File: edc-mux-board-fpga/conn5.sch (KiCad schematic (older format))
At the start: 24 parts, among them U19 MAX4910, U20 TLV320AIC3206, U21 P82B96

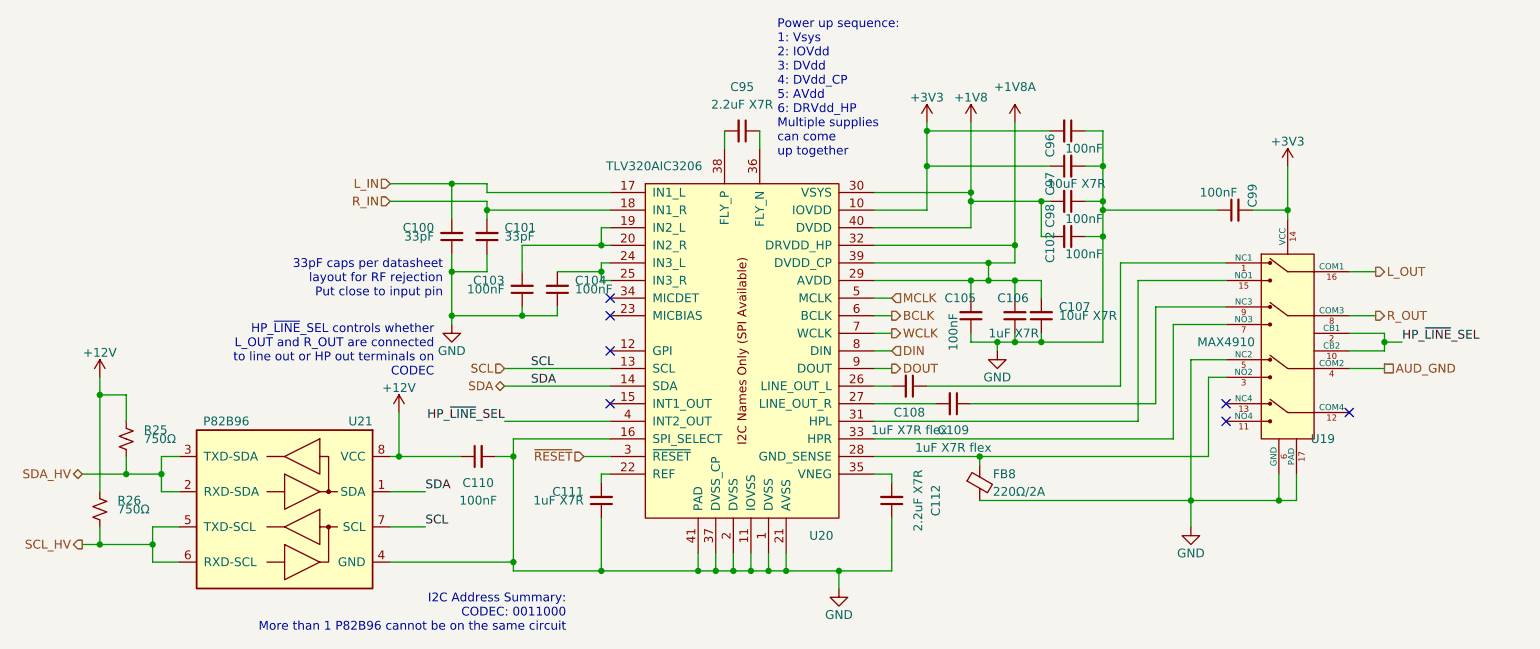
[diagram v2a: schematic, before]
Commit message: re-annotating after adding power ICs and decoupling capacitors.
Also verified most footprints, and updated schematic field data.
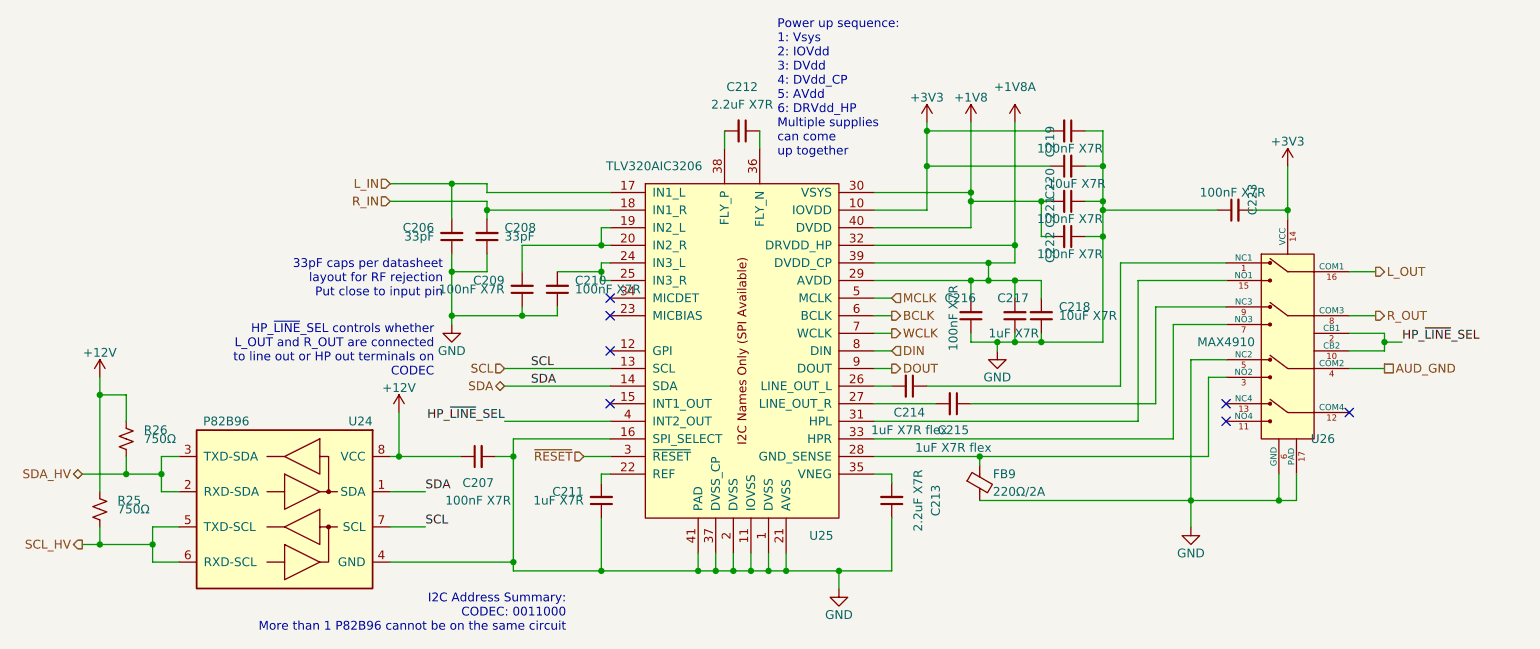
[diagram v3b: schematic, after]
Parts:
- C207: renamed from C110; value 100nF -> 100nF X7R
- C209: renamed from C103; value 100nF -> 100nF X7R
- C210: renamed from C104; value 100nF -> 100nF X7R
- C216: renamed from C105; value 100nF -> 100nF X7R
- C219: renamed from C96; value 100nF -> 100nF X7R
- C221: renamed from C98; value 100nF -> 100nF X7R
- C222: renamed from C102; value 100nF -> 100nF X7R
- C223: renamed from C99; value 100nF -> 100nF X7R
- R25: renamed from R26; Package ID (none) -> 0402in/1005mm
- R26: renamed from R25; Package ID (none) -> 0402in/1005mm
- renumbered C100 to C206, C101 to C208, C111 to C211, C95 to C212, C112 to C213, C108 to C214, C109 to C215, C106 to C217, C107 to C218, C97 to C220, FB8 to FB9, U21 to U24, U20 to U25, U19 to U26

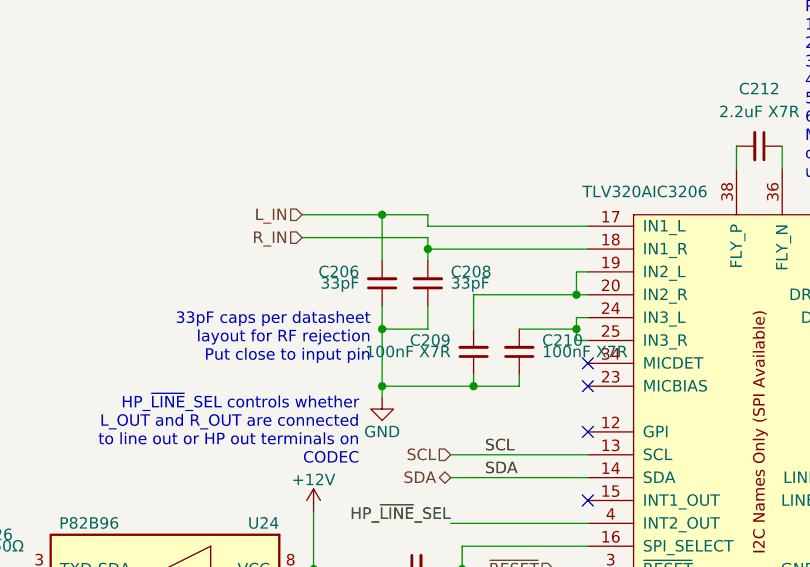
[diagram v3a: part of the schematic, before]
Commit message: Reannotating and adding more fields to components
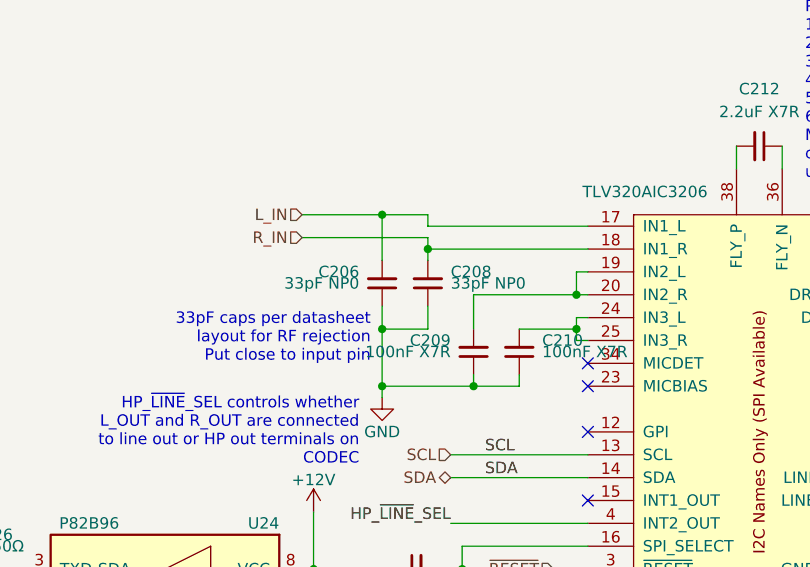
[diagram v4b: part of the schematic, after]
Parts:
- C206, C208: value 33pF -> 33pF NP0; footprint Capacitor_SMD:C_0603_1608Metric -> Capacitor_SMD:C_0402_1005Metric; Characteristics (none) -> CAP CER 33PF 25V NP0 0402; Description (none) -> MLCC Capacitor; Manufacturer (none) -> AVX; Manufacturers Part Number (none) -> 04023A330FAT2A; Package ID 0603in/1608mm -> 0402in/1005mm
- C207, C209, C210, C216, C219, C221, C222, C223: Characteristics (none) -> CAP CER 0.1UF 25V X7R 0603; Description (none) -> MLCC Capacitor; Manufacturer (none) -> Kemet; Manufacturers Part Number (none) -> C0603C104J3RACAUTO
- C211, C217: Characteristics (none) -> CAP CER 1UF 25V X7R 0603; Description (none) -> MLCC Capacitor
- C212, C213: footprint Capacitor_SMD:C_0603_1608Metric -> Capacitor_SMD:C_0805_2012Metric; Characteristics (none) -> CAP CER 2.2UF 25V X7R 0805; Description (none) -> MLCC Capacitor; Manufacturer (none) -> TDK; Manufacturers Part Number (none) -> CGA4J3X7R1E225K125AB; Package ID 0603in/1608mm -> 0805in/2012mm
- C214, C215: Characteristics (none) -> CAP CER 0805 1UF 25V X7R 5%; Description (none) -> MLCC Capacitor; Manufacturers Part Number C0805X105J3RACAUTO -> C0805X105J3RECAUTO
- C218, C220: Characteristics (none) -> CAP CER 10UF 25V X7R 1206; Description (none) -> MLCC Capacitor
- FB9: footprint Resistor_SMD:R_0603_1608Metric -> Inductor_SMD:L_0603_1608Metric; Description (none) -> Ferrite Bead
- R25, R26: Description (none) -> Resistor
- U24: Description (none) -> I2C Buffer / Voltage Translator; Manufacturer (none) -> Texas Instruments; Manufacturers Part Number (none) -> P82B96; Package ID (none) -> TSSOP8
- U25: Description (none) -> I2S Audio Codec; Manufacturer (none) -> Texas Instruments; Package ID (none) -> UQFN40
- U26: Description (none) -> Clickless Audio Switch; Manufacturer (none) -> Maxim Integrated; Package ID (none) -> TQFN16

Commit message: Fixed resistor footprint
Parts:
- R25, R26: footprint Resistor_SMD:R_0603_1608Metric -> Resistor_SMD:R_0402_1005Metric
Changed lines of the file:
@@
 F 0 "R26" H 1800 3950 50  0000 L CNN
 F 1 "750Ω" H 1800 3900 50  0000 L CNN
-F 2 "Resistor_SMD:R_0603_1608Metric" H 1700 3900 50  0001 C CNN
+F 2 "Resistor_SMD:R_0402_1005Metric" H 1700 3900 50  0001 C CNN
 F 3 "~" H 1700 3900 50  0001 C CNN
 F 4 "0402in/1005mm" H 0   0   50  0001 C CNN "Package ID"
@@
 F 0 "R25" H 1650 4350 50  0000 L CNN
 F 1 "750Ω" H 1650 4300 50  0000 L CNN
-F 2 "Resistor_SMD:R_0603_1608Metric" H 1550 4300 50  0001 C CNN
+F 2 "Resistor_SMD:R_0402_1005Metric" H 1550 4300 50  0001 C CNN
 F 3 "~" H 1550 4300 50  0001 C CNN
 F 4 "0402in/1005mm" H 0   0   50  0001 C CNN "Package ID"
